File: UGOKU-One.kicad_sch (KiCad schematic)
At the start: 53 parts, among them J1 PB0, J2 PA10, J3 Conn_01x02_Male, J6 Conn_01x04, SW1 PF1, SW2 RESET, SW3 SW_Push_DPDT, SW5 SW_Push_DPDT, T1 PTS_1.5_2, T3 PTS_1.5_2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

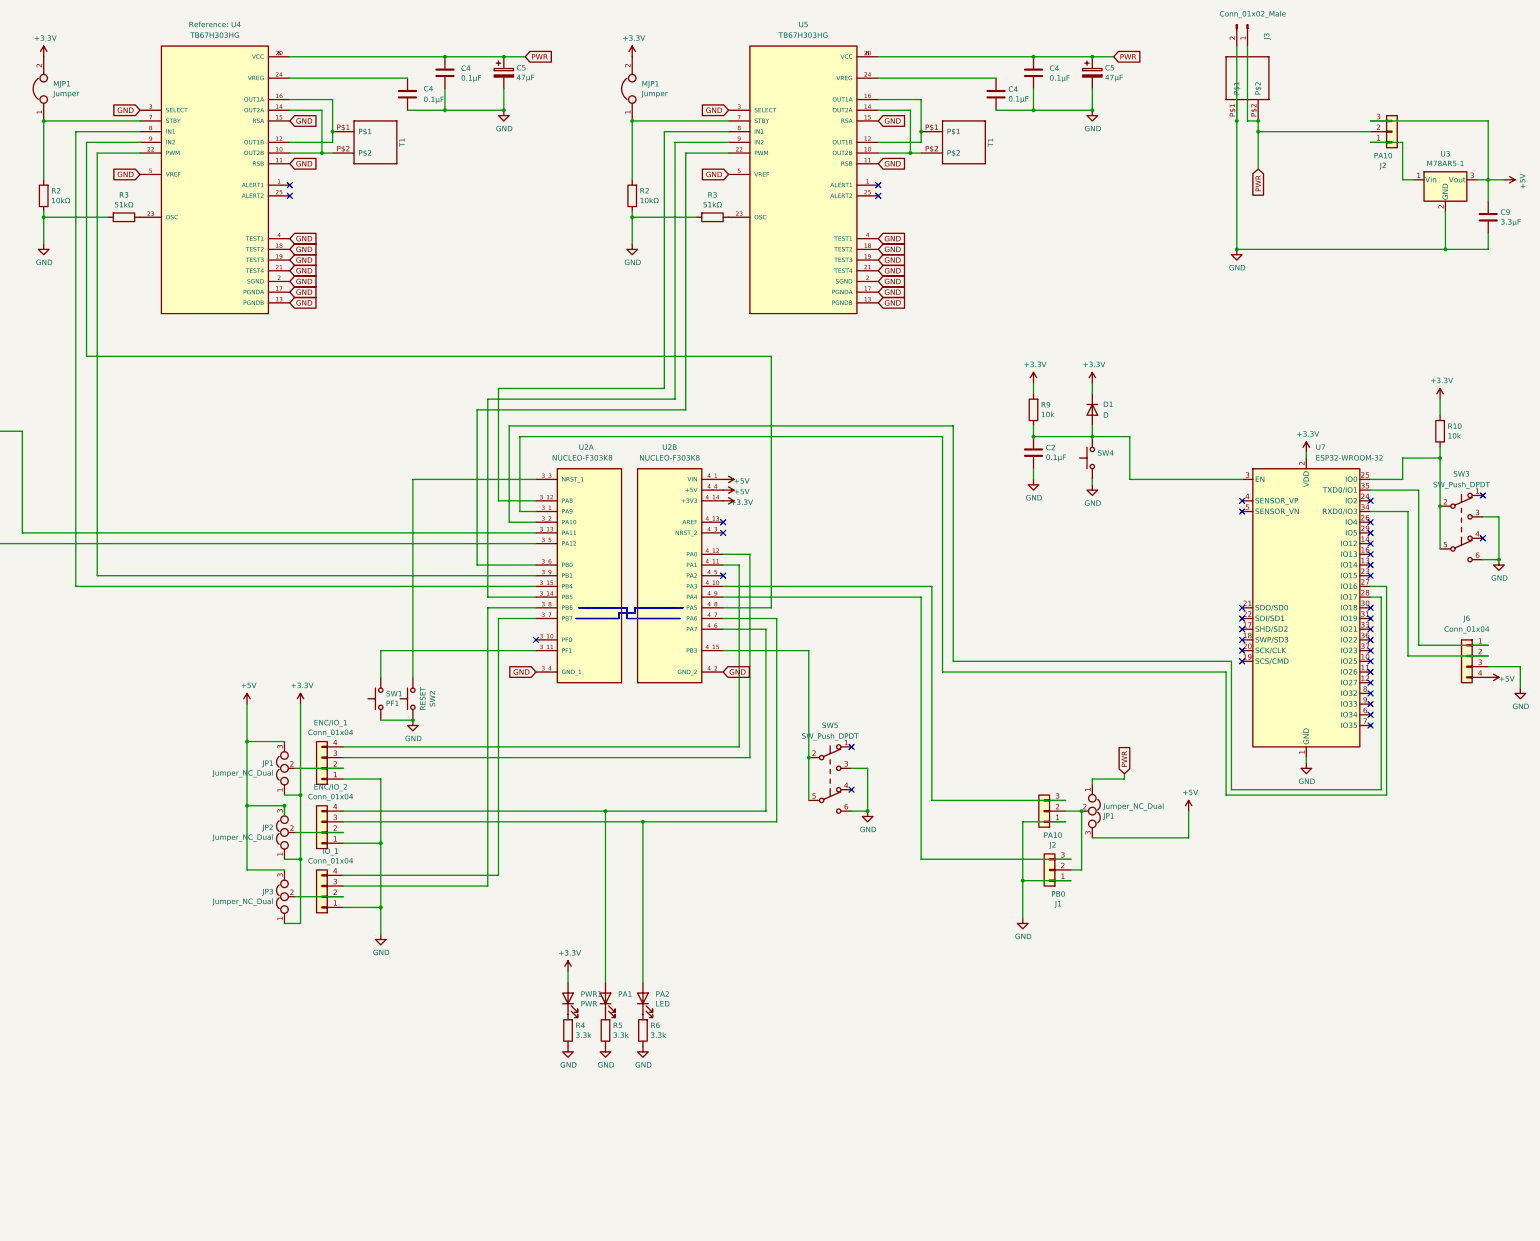
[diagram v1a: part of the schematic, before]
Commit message: Motor driver STM pin assignment replacement
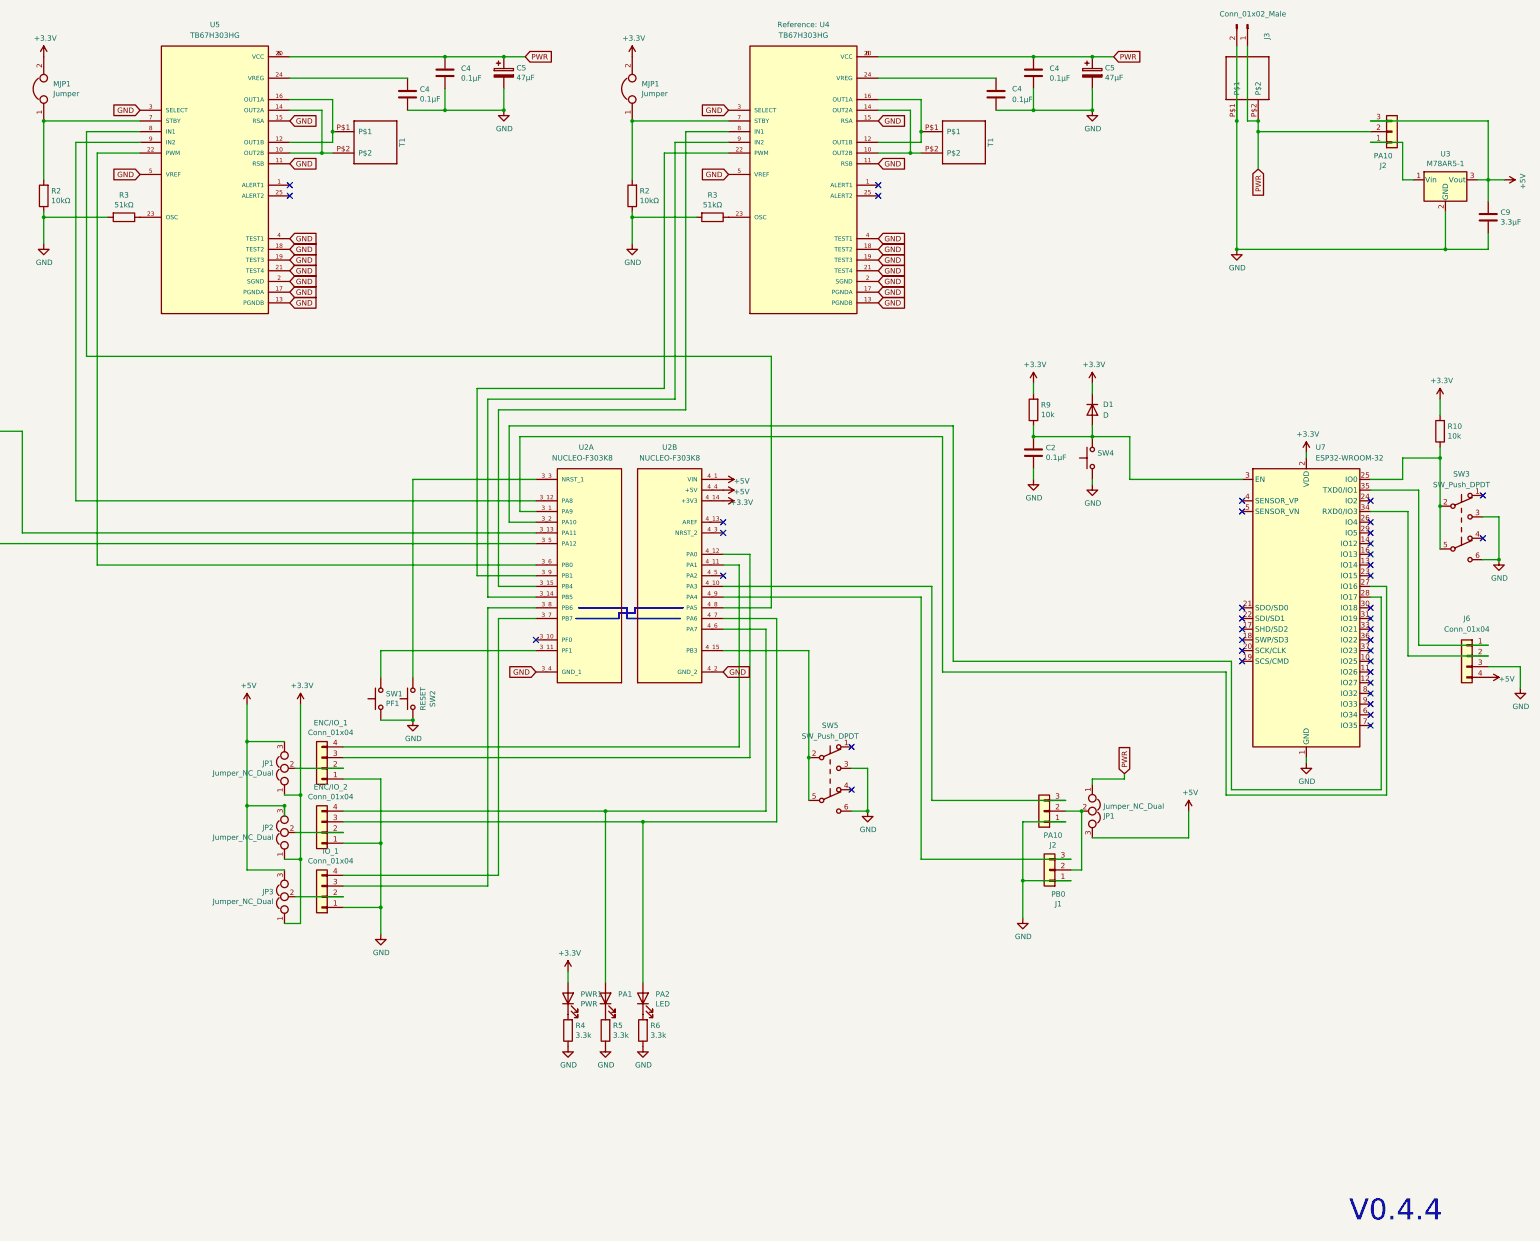
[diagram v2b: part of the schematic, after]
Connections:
- net at U2.3_12 (PA8): now also U5.9 (IN2); no longer U5.8 (IN1)
- net at U2.3_14 (PB5): now also U4.9 (IN2); no longer U5.9 (IN2)
- net at U2.4_8 (PA5): now also U5.8 (IN1); no longer U4.9 (IN2)
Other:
- note added: "V0.4.4"
- moved on the sheet: C4, C5, MJP1, R2, R3, Reference: U4, T1, U5

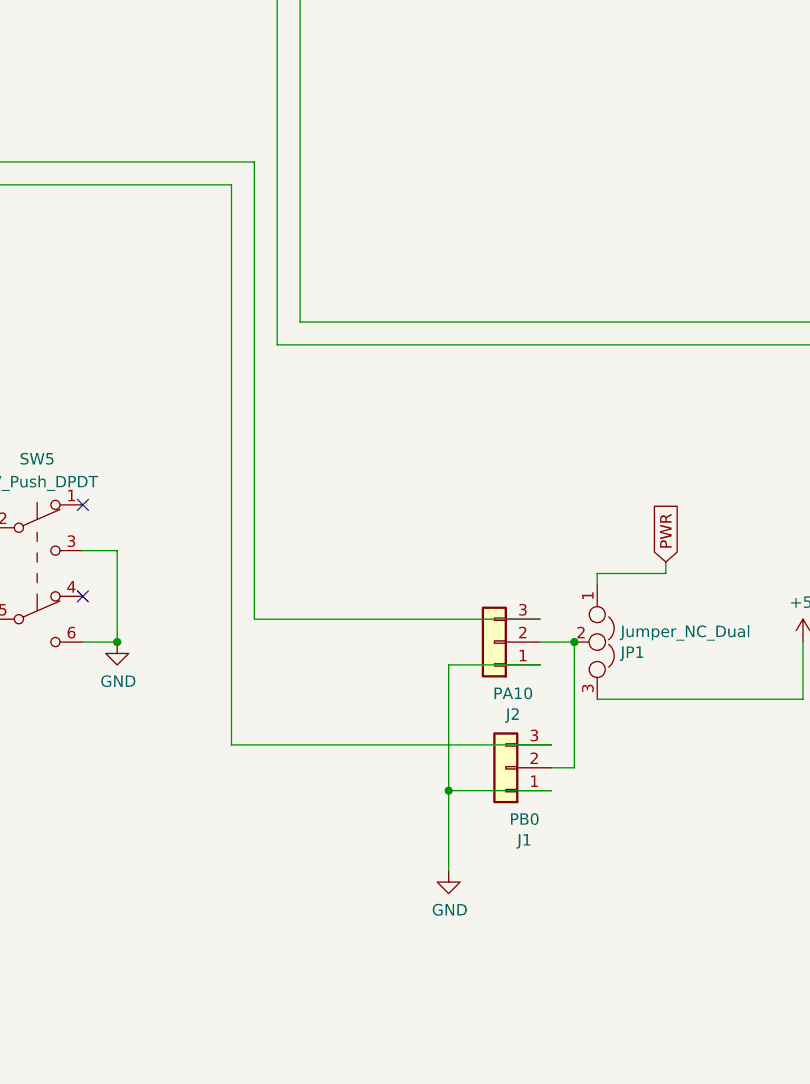
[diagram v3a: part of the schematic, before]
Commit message: Update Diode footprint and servo pin header
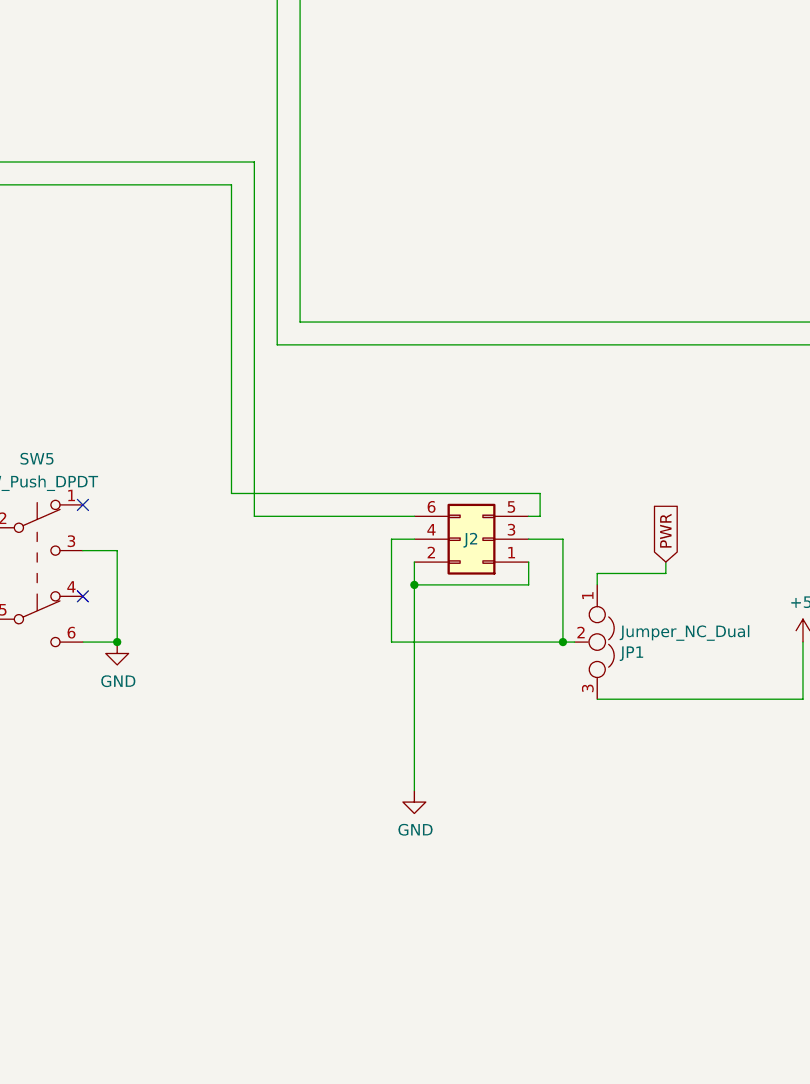
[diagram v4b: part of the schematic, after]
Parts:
- removed J1: PB0, Connector_PinHeader_2.54mm:PinHeader_1x03_P2.54mm_Vertical, symbol Connector_Generic:Conn_01x03
- removed J2: PA10, Connector_PinHeader_2.54mm:PinHeader_1x03_P2.54mm_Vertical, symbol Connector_Generic:Conn_01x03
- added J2: Conn_02x03_Odd_Even, Connector_PinHeader_2.54mm:PinHeader_2x03_P2.54mm_Vertical, symbol Connector_Generic:Conn_02x03_Odd_Even
- D1: footprint Diode_SMD:D_SOD-123F -> Diode_SMD:D_SOD-123
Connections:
- net GND: now also J2.1 (Pin_1), J2.2 (Pin_2)
- net at JP1.2: now also J2.3 (Pin_3), J2.4 (Pin_4)
- net at U2.4_9 (PA4): now also J2.5 (Pin_5)
- net at U2.4_10 (PA3): now also J2.6 (Pin_6)

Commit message: IOコネクタを圧着不要コネクタhar-flexicon化する検討を開始
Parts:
- CAN1: footprint Connector_JST:JST_XA_B03B-XASK-1_1x03_P2.50mm_Vertical -> UGOKU-One_Libraries:har-flexicon_2.54_3pin
- ENC/IO_1, ENC/IO_2, IO_1: footprint Connector_JST:JST_XA_B04B-XASK-1_1x04_P2.50mm_Vertical -> UGOKU-One_Libraries:har-flexicon_2.54_4pin
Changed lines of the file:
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@@
       (effects (font (size 1.27 1.27)))
     )
-    (property "Footprint" "Connector_JST:JST_XA_B04B-XASK-1_1x04_P2.50mm_Vertical" (at 233.68 293.37 0)
+    (property "Footprint" "UGOKU-One_Libraries:har-flexicon_2.54_4pin" (at 233.68 293.37 0)
       (effects (font (size 1.27 1.27)) hide)
     )
@@
       (effects (font (size 1.27 1.27)))
     )
-    (property "Footprint" "Connector_JST:JST_XA_B04B-XASK-1_1x04_P2.50mm_Vertical" (at 233.68 278.13 0)
+    (property "Footprint" "UGOKU-One_Libraries:har-flexicon_2.54_4pin" (at 233.68 278.13 0)
       (effects (font (size 1.27 1.27)) hide)
     )
@@
       (project "UGOKU-One"
         (path "/f89d8039-fb4d-432a-bf6a-fadbc30a6f09"
-          (reference "CN3") (unit 1)
+          (reference "CN1") (unit 1)
         )
       )
@@
       (effects (font (size 1.27 1.27)))
     )
-    (property "Footprint" "Connector_JST:JST_XA_B03B-XASK-1_1x03_P2.50mm_Vertical" (at 71.12 187.96 0)
+    (property "Footprint" "UGOKU-One_Libraries:har-flexicon_2.54_3pin" (at 71.12 187.96 0)
       (effects (font (size 1.27 1.27)) hide)
     )
@@
       (effects (font (size 1.27 1.27)))
     )
-    (property "Footprint" "Connector_JST:JST_XA_B04B-XASK-1_1x04_P2.50mm_Vertical" (at 233.68 308.61 0)
+    (property "Footprint" "UGOKU-One_Libraries:har-flexicon_2.54_4pin" (at 233.68 308.61 0)
       (effects (font (size 1.27 1.27)) hide)
     )
@@
       (project "UGOKU-One"
         (path "/f89d8039-fb4d-432a-bf6a-fadbc30a6f09"
-          (reference "CN1") (unit 1)
-        )
-      )
+          (reference "CN3") (unit 1)
+        )
+      )
